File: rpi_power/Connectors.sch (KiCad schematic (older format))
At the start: 6 parts, among them J1 POWER, J2 Raspberry_Pi_2_3, J3 Raspberry_Pi_2_3, J4 ADCs, J7 PROG, J9 GPIO

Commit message: Components placed.
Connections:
- net GPIO0: now also J9.6 (Pin_6); no longer J9.2 (Pin_2)
- net GPIO1: now also J9.5 (Pin_5); no longer J9.3 (Pin_3)
- net GPIO3: now also J9.3 (Pin_3); no longer J9.5 (Pin_5)
- net GPIO4: now also J9.2 (Pin_2); no longer J9.6 (Pin_6)
- net ADC1 renamed ADC3_IN
- net ADC2 renamed ADC2_IN
- net ADC3 renamed ADC1_IN
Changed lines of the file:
@@
 Wire Wire Line
 	4950 5750 5150 5750
+Text GLabel 5150 5550 2    50   Output ~ 0
+ADC1_IN
+Text GLabel 5150 5650 2    50   Output ~ 0
+ADC2_IN
 Text GLabel 5150 5750 2    50   Output ~ 0
-ADC1
-Text GLabel 5150 5650 2    50   Output ~ 0
-ADC2
-Text GLabel 5150 5550 2    50   Output ~ 0
-ADC3
+ADC3_IN
 $Comp
 L Connector:Conn_01x06_Male J?
@@
 Wire Wire Line
 	7500 5450 7650 5450
-Text GLabel 7650 5850 2    50   BiDi ~ 0
+Text GLabel 7650 5450 2    50   BiDi ~ 0
 GPIO0
 $Comp
@@
 	-1   0    0    1
 $EndComp
-Text GLabel 7650 5750 2    50   BiDi ~ 0
+Text GLabel 7650 5550 2    50   BiDi ~ 0
 GPIO1
 Text GLabel 7650 5650 2    50   BiDi ~ 0
 GPIO2
-Text GLabel 7650 5550 2    50   BiDi ~ 0
+Text GLabel 7650 5750 2    50   BiDi ~ 0
 GPIO3
-Text GLabel 7650 5450 2    50   BiDi ~ 0
+Text GLabel 7650 5850 2    50   BiDi ~ 0
 GPIO4
 Text GLabel 4100 1750 2    50   UnSpc ~ 0

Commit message: Routing done, pending review.
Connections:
- net +3V3 renamed 1
- net 1: no longer J2.17 (3V3), J3.17 (3V3)
- new net 17: J2.17 (3V3), J3.17 (3V3)
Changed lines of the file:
@@
 	2850 1350 2850 1300
-Wire Wire Line
-	3150 1350 3150 1300
-Wire Wire Line
-	3250 1350 3250 1300
 Wire Wire Line
 	3850 1750 4100 1750
@@
 	2850 1300 2900 1300
 Wire Wire Line
-	3150 1300 3200 1300
-Wire Wire Line
 	2950 1300 2950 1350
 Wire Wire Line
@@
 Wire Wire Line
 	2900 1300 2950 1300
-Wire Wire Line
-	3200 1300 3200 1250
-Connection ~ 3200 1300
-Wire Wire Line
-	3200 1300 3250 1300
 $Comp
 L power:+5V #PWR03
@@
 F 3 "" H 2900 1250 50  0001 C CNN
 	1    2900 1250
-	1    0    0    -1
-$EndComp
-$Comp
-L power:+3V3 #PWR05
-U 1 1 5BE0BE90
-P 3200 1250
-F 0 "#PWR05" H 3200 1100 50  0001 C CNN
-F 1 "+3V3" H 3215 1423 50  0000 C CNN
-F 2 "" H 3200 1250 50  0001 C CNN
-F 3 "" H 3200 1250 50  0001 C CNN
-	1    3200 1250
 	1    0    0    -1
 $EndComp
@@
 Text GLabel 4100 2150 2    50   BiDi ~ 0
 I2C_SCL
-Wire Wire Line
-	3250 1300 3550 1300
-Connection ~ 3250 1300
-$Comp
-L power:PWR_FLAG #FLG03
-U 1 1 5BE8CB1B
-P 3550 1300
-F 0 "#FLG03" H 3550 1375 50  0001 C CNN
-F 1 "PWR_FLAG" H 3550 1474 50  0000 C CNN
-F 2 "" H 3550 1300 50  0001 C CNN
-F 3 "~" H 3550 1300 50  0001 C CNN
-	1    3550 1300
-	1    0    0    -1
-$EndComp
 $Comp
 L Connector_Generic:Conn_01x03 J1
@@
 	7400 1400 7400 1350
 Wire Wire Line
-	7700 1400 7700 1350
-Wire Wire Line
-	7800 1400 7800 1350
-Wire Wire Line
 	8400 1800 8650 1800
 Wire Wire Line
@@
 	7400 1350 7450 1350
 Wire Wire Line
-	7700 1350 7750 1350
-Wire Wire Line
 	7500 1350 7500 1400
 Wire Wire Line
@@
 Wire Wire Line
 	7450 1350 7500 1350
-Wire Wire Line
-	7750 1350 7750 1300
-Connection ~ 7750 1350
-Wire Wire Line
-	7750 1350 7800 1350
 $Comp
 L power:+5V #PWR014
@@
 F 3 "" H 7450 1300 50  0001 C CNN
 	1    7450 1300
-	1    0    0    -1
-$EndComp
-$Comp
-L power:+3V3 #PWR016
-U 1 1 5BEE7F48
-P 7750 1300
-F 0 "#PWR016" H 7750 1150 50  0001 C CNN
-F 1 "+3V3" H 7765 1473 50  0000 C CNN
-F 2 "" H 7750 1300 50  0001 C CNN
-F 3 "" H 7750 1300 50  0001 C CNN
-	1    7750 1300
 	1    0    0    -1
 $EndComp
@@
 Wire Wire Line
 	7650 5950 7650 6000
+Text GLabel 3150 1150 1    50   UnSpc ~ 0
+1
+Text GLabel 3250 1150 1    50   UnSpc ~ 0
+17
+Text GLabel 7700 1400 1    50   UnSpc ~ 0
+1
+Text GLabel 7800 1400 1    50   UnSpc ~ 0
+17
+Wire Wire Line
+	3150 1350 3150 1200
+Wire Wire Line
+	3250 1150 3250 1300
+$Comp
+L power:PWR_FLAG #FLG0101
+U 1 1 5BDC6759
+P 3400 1300
+F 0 "#FLG0101" H 3400 1375 50  0001 C CNN
+F 1 "PWR_FLAG" V 3400 1428 50  0000 L CNN
+F 2 "" H 3400 1300 50  0001 C CNN
+F 3 "~" H 3400 1300 50  0001 C CNN
+	1    3400 1300
+	0    1    1    0
+$EndComp
+Connection ~ 3250 1300
+Wire Wire Line
+	3250 1300 3250 1350
+$Comp
+L power:PWR_FLAG #FLG0102
+U 1 1 5BDC677F
+P 3400 1200
+F 0 "#FLG0102" H 3400 1275 50  0001 C CNN
+F 1 "PWR_FLAG" V 3400 1328 50  0000 L CNN
+F 2 "" H 3400 1200 50  0001 C CNN
+F 3 "~" H 3400 1200 50  0001 C CNN
+	1    3400 1200
+	0    1    1    0
+$EndComp
+Wire Wire Line
+	3250 1300 3400 1300
+Wire Wire Line
+	3400 1200 3150 1200
+Connection ~ 3150 1200
+Wire Wire Line
+	3150 1200 3150 1150
 $EndSCHEMATC

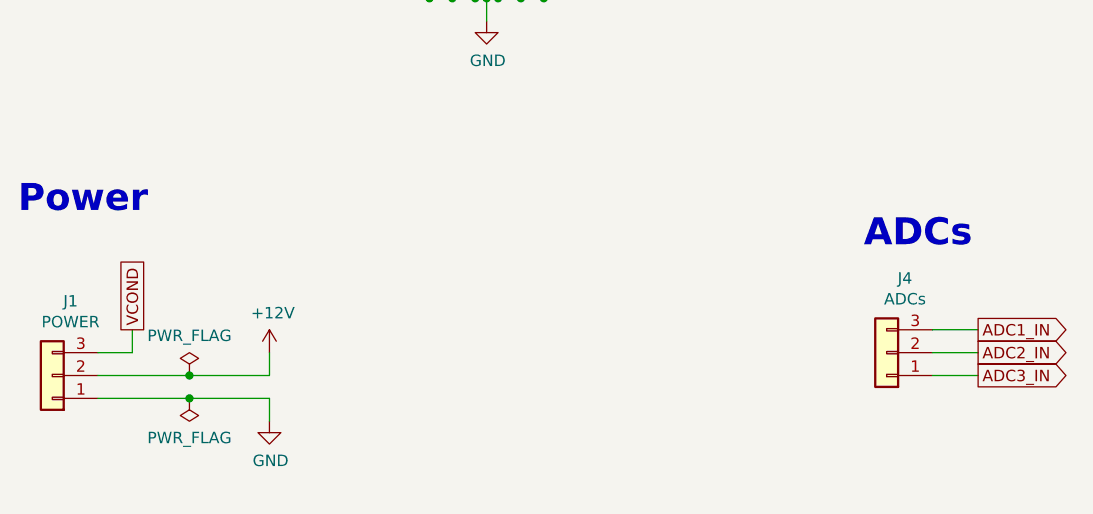
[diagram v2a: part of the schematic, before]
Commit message: Differentiated VCOND and BATT+. Routing done.
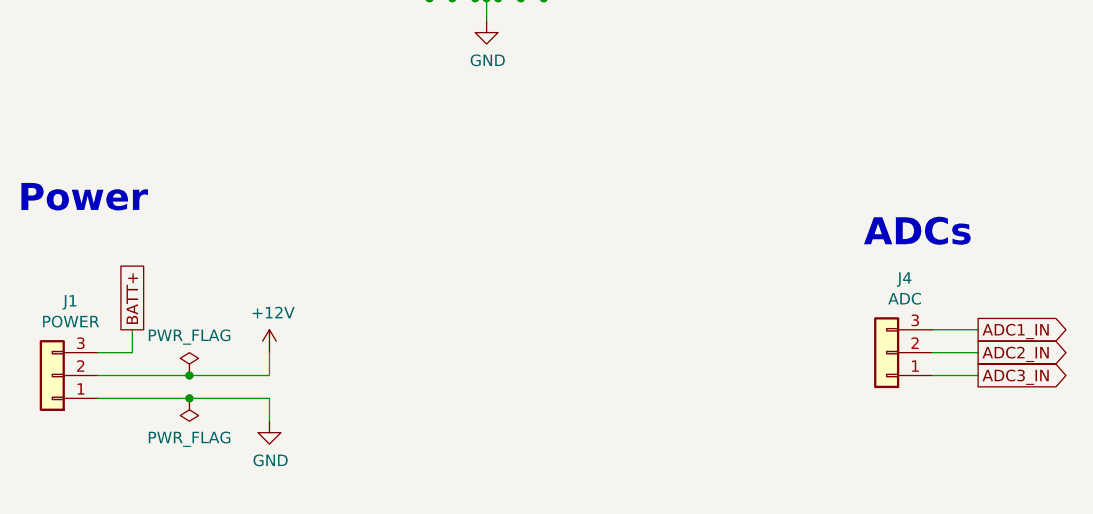
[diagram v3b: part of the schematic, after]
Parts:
- J4: value ADCs -> ADC
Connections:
- net VCOND renamed BATT+
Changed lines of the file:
@@
 	1450 5650 1450 5550
 Text GLabel 1450 5550 1    50   UnSpc ~ 0
-VCOND
+BATT+
 $Comp
 L power:PWR_FLAG #FLG01
@@
 P 4750 5650
 F 0 "J4" H 4670 5325 50  0000 C CNN
-F 1 "ADCs" H 4670 5416 50  0000 C CNN
+F 1 "ADC" H 4670 5416 50  0000 C CNN
 F 2 "w_conn_mpt:mpt_0,5-3-2,54" H 4750 5650 50  0001 C CNN
 F 3 "~" H 4750 5650 50  0001 C CNN
